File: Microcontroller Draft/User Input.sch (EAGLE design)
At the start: 8 parts

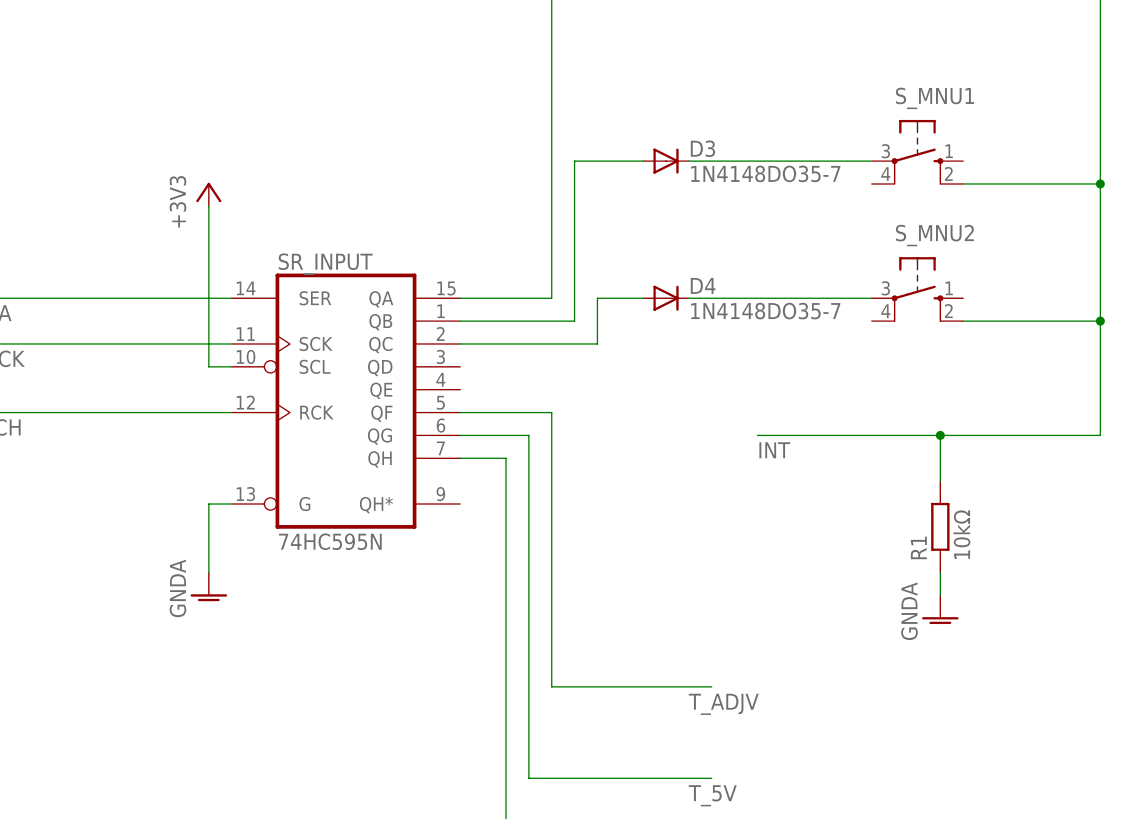
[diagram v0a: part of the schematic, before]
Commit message: Added the LCD schematic
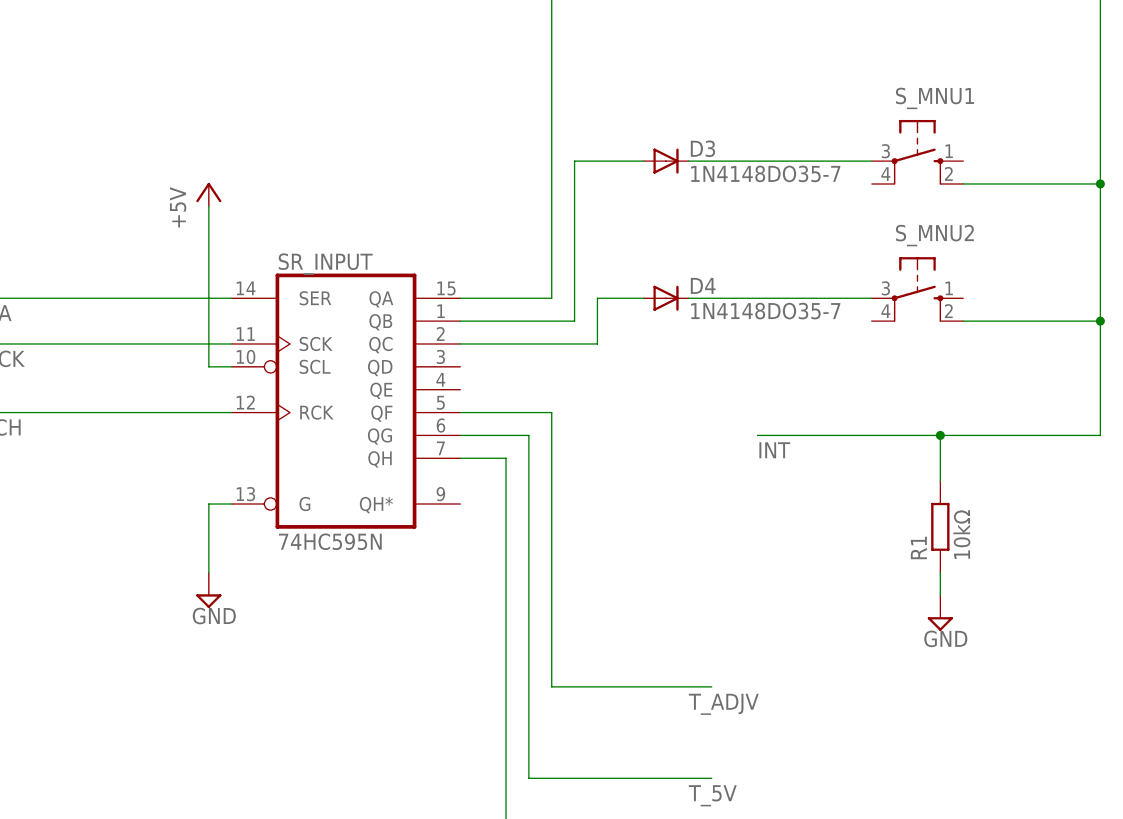
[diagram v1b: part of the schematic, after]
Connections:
- net +3V3 renamed +5V
- net GNDA renamed GND
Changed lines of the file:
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@@
 <part name="SR_INPUT" library="74xx-eu" deviceset="74*595" device="N" technology="HC"/>
 <part name="R1" library="resistor" deviceset="R-EU_" device="0207/10" value="10kΩ"/>
-<part name="GND1" library="supply1" deviceset="GNDA" device=""/>
 <part name="D2" library="diode" deviceset="1N4148" device="DO35-7"/>
 <part name="D3" library="diode" deviceset="1N4148" device="DO35-7"/>
 <part name="D4" library="diode" deviceset="1N4148" device="DO35-7"/>
-<part name="GND2" library="supply1" deviceset="GNDA" device=""/>
-<part name="+3V1" library="supply1" deviceset="+3V3" device=""/>
+<part name="SUPPLY1" library="supply2" deviceset="GND" device=""/>
+<part name="SUPPLY2" library="supply2" deviceset="GND" device=""/>
+<part name="P+1" library="supply1" deviceset="+5V" device=""/>
 </parts>
 <sheets>
@@
 <instance part="SR_INPUT" gate="A" x="50.8" y="109.22"/>
 <instance part="R1" gate="G$1" x="116.84" y="93.98" rot="R90"/>
-<instance part="GND1" gate="1" x="116.84" y="83.82"/>
 <instance part="D2" gate="G$1" x="86.36" y="160.02"/>
 <instance part="D3" gate="G$1" x="86.36" y="134.62"/>
 <instance part="D4" gate="G$1" x="86.36" y="119.38"/>
-<instance part="GND2" gate="1" x="35.56" y="86.36"/>
-<instance part="+3V1" gate="G$1" x="35.56" y="132.08"/>
+<instance part="SUPPLY1" gate="GND" x="35.56" y="86.36"/>
+<instance part="SUPPLY2" gate="GND" x="116.84" y="83.82"/>
+<instance part="P+1" gate="1" x="35.56" y="132.08"/>
 </instances>
 <busses>
@@
 <label x="96.52" y="101.6" size="1.778" layer="95"/>
 <junction x="116.84" y="104.14"/>
-</segment>
-</net>
-<net name="+3V3" class="0">
-<segment>
-<pinref part="+3V1" gate="G$1" pin="+3V3"/>
-<pinref part="SR_INPUT" gate="A" pin="SCL"/>
-<wire x1="35.56" y1="129.54" x2="35.56" y2="111.76" width="0.1524" layer="91"/>
-<wire x1="35.56" y1="111.76" x2="38.1" y2="111.76" width="0.1524" layer="91"/>
-</segment>
-</net>
-<net name="GNDA" class="0">
-<segment>
-<pinref part="GND1" gate="1" pin="GNDA"/>
-<pinref part="R1" gate="G$1" pin="1"/>
-<wire x1="116.84" y1="86.36" x2="116.84" y2="88.9" width="0.1524" layer="91"/>
-</segment>
-<segment>
-<pinref part="SR_INPUT" gate="A" pin="G"/>
-<pinref part="GND2" gate="1" pin="GNDA"/>
-<wire x1="38.1" y1="96.52" x2="35.56" y2="96.52" width="0.1524" layer="91"/>
-<wire x1="35.56" y1="96.52" x2="35.56" y2="88.9" width="0.1524" layer="91"/>
 </segment>
 </net>
@@
 </segment>
 </net>
+<net name="GND" class="0">
+<segment>
+<pinref part="SR_INPUT" gate="A" pin="G"/>
+<wire x1="38.1" y1="96.52" x2="35.56" y2="96.52" width="0.1524" layer="91"/>
+<wire x1="35.56" y1="96.52" x2="35.56" y2="88.9" width="0.1524" layer="91"/>
+<pinref part="SUPPLY1" gate="GND" pin="GND"/>
+</segment>
+<segment>
+<pinref part="R1" gate="G$1" pin="1"/>
+<wire x1="116.84" y1="86.36" x2="116.84" y2="88.9" width="0.1524" layer="91"/>
+<pinref part="SUPPLY2" gate="GND" pin="GND"/>
+</segment>
+</net>
+<net name="+5V" class="0">
+<segment>
+<pinref part="SR_INPUT" gate="A" pin="SCL"/>
+<wire x1="35.56" y1="129.54" x2="35.56" y2="111.76" width="0.1524" layer="91"/>
+<wire x1="35.56" y1="111.76" x2="38.1" y2="111.76" width="0.1524" layer="91"/>
+<pinref part="P+1" gate="1" pin="+5V"/>
+</segment>
+</net>

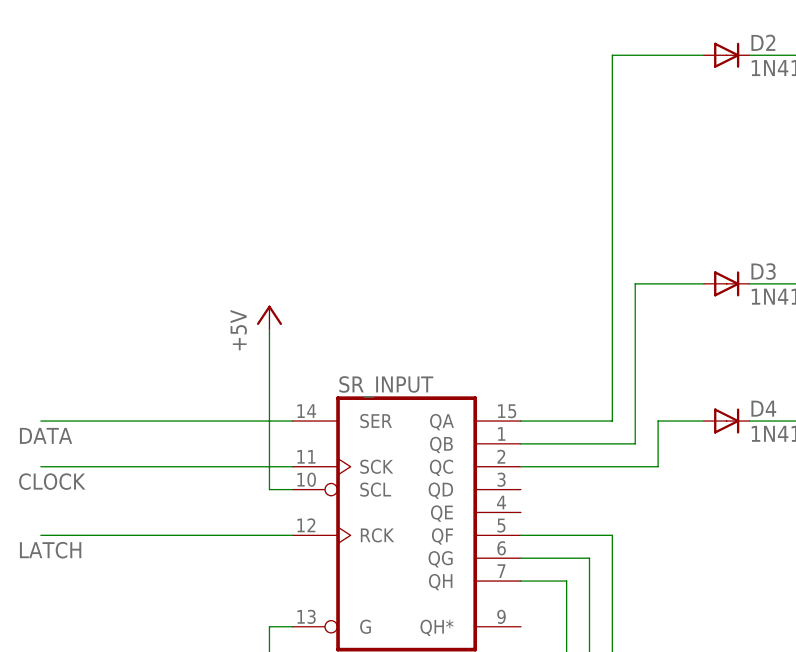
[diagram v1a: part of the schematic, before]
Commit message: Finished the individual schematics
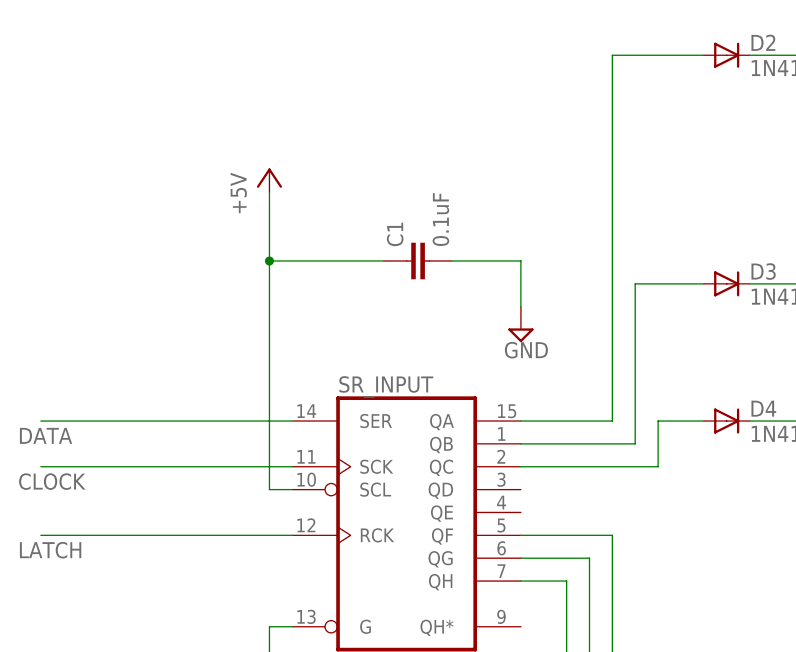
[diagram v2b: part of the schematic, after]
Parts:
- added C1: 0.1uF, rcl:C-EU025-025X050
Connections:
- net +5V: now also C1.1
- net GND: now also C1.2
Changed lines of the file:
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@@
 <part name="SUPPLY2" library="supply2" deviceset="GND" device=""/>
 <part name="P+1" library="supply1" deviceset="+5V" device=""/>
+<part name="C1" library="rcl" deviceset="C-EU" device="025-025X050" value="0.1uF"/>
+<part name="SUPPLY3" library="supply2" deviceset="GND" device=""/>
 </parts>
 <sheets>
@@
 <instance part="SUPPLY1" gate="GND" x="35.56" y="86.36"/>
 <instance part="SUPPLY2" gate="GND" x="116.84" y="83.82"/>
-<instance part="P+1" gate="1" x="35.56" y="132.08"/>
+<instance part="P+1" gate="1" x="35.56" y="147.32"/>
+<instance part="C1" gate="G$1" x="50.8" y="137.16" rot="R90"/>
+<instance part="SUPPLY3" gate="GND" x="63.5" y="129.54"/>
 </instances>
 <busses>
@@
 <pinref part="SUPPLY2" gate="GND" pin="GND"/>
 </segment>
+<segment>
+<pinref part="C1" gate="G$1" pin="2"/>
+<pinref part="SUPPLY3" gate="GND" pin="GND"/>
+<wire x1="55.88" y1="137.16" x2="63.5" y2="137.16" width="0.1524" layer="91"/>
+<wire x1="63.5" y1="137.16" x2="63.5" y2="132.08" width="0.1524" layer="91"/>
+</segment>
 </net>
 <net name="+5V" class="0">
 <segment>
 <pinref part="SR_INPUT" gate="A" pin="SCL"/>
-<wire x1="35.56" y1="129.54" x2="35.56" y2="111.76" width="0.1524" layer="91"/>
+<wire x1="35.56" y1="144.78" x2="35.56" y2="137.16" width="0.1524" layer="91"/>
+<wire x1="35.56" y1="137.16" x2="35.56" y2="111.76" width="0.1524" layer="91"/>
 <wire x1="35.56" y1="111.76" x2="38.1" y2="111.76" width="0.1524" layer="91"/>
 <pinref part="P+1" gate="1" pin="+5V"/>
+<pinref part="C1" gate="G$1" pin="1"/>
+<wire x1="48.26" y1="137.16" x2="35.56" y2="137.16" width="0.1524" layer="91"/>
+<junction x="35.56" y="137.16"/>
 </segment>
 </net>

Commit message: Fixed some errors
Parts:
- removed C1: 0.1uF, rcl:C-EU025-025X050
- removed R1: 10kΩ, resistor:R-EU_0207/10
- added C10: 0.1uF, rcl:C-EU025-025X050
- added R3: 10kΩ, resistor:R-EU_0207/10
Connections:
- net +5V: now also C10.2, SR_INPUTP.VCC; no longer C1.1
- net GND: now also C10.1, R3.1, SR_INPUTP.GND; no longer C1.2, R1.1
- net INT: now also R3.2; no longer R1.2
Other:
- moved on the sheet: D2, D3, D4, SR_INPUT, S_MNU1, S_MNU2, S_PWR

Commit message: Added the rotary encoder to the mix
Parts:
- added RE1: ECW1J-B24-BCCO24LECW1J-B, Custom Stuff:ECW1J-B24-BCCO24LECW1J-B
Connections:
- new net RE_A: RE1.A
- new net RE_B: RE1.B
- net +5V: now also RE1.C
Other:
- moved on the sheet: C10, D2, D3, D4, R3, SR_INPUT, SR_INPUTP, S_MNU1, S_MNU2, S_PWR
